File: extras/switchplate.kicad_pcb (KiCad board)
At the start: 2 copper layers, 344.4 x 121.3 mm, 2 parts

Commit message: update gerbers to latest kicad version defaults
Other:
- rule pad_to_mask_clearance: 0.05 -> 0

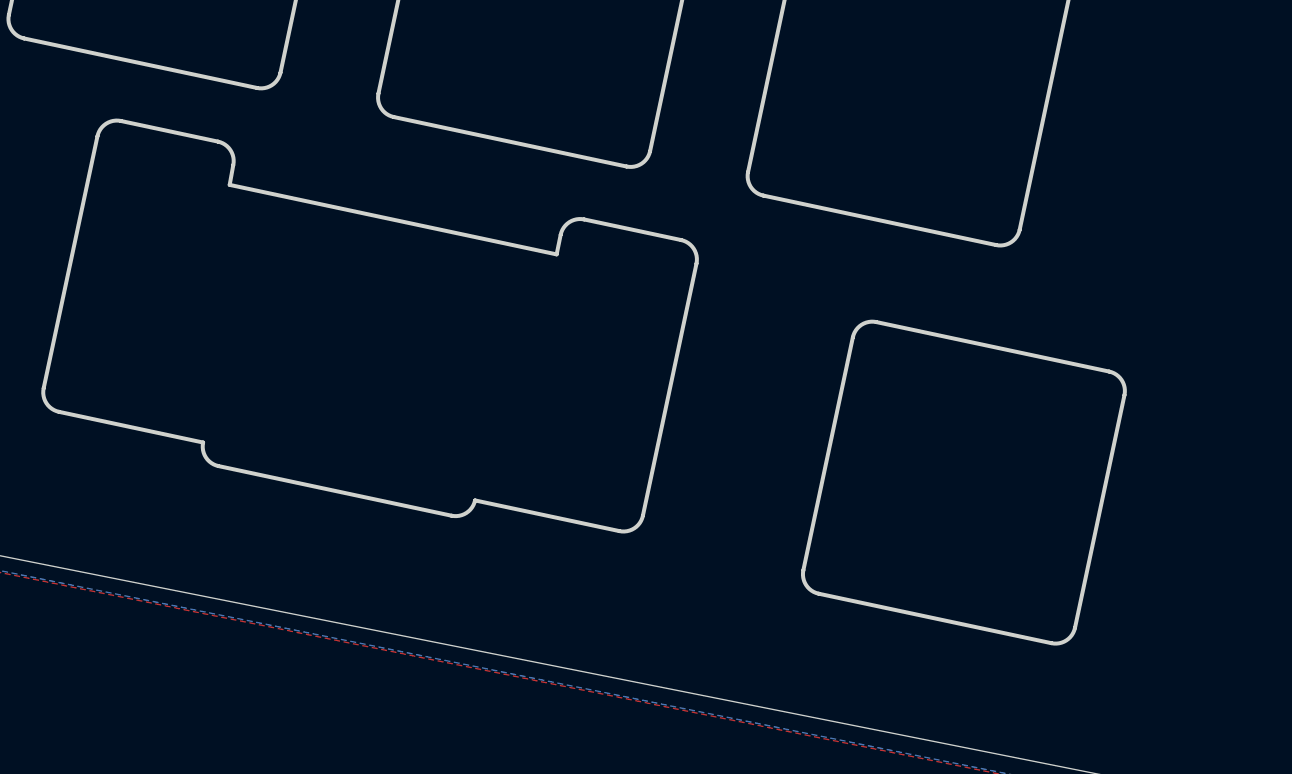
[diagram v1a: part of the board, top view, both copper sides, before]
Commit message: add 2.25u left space support and update caps to use cftkb footprints
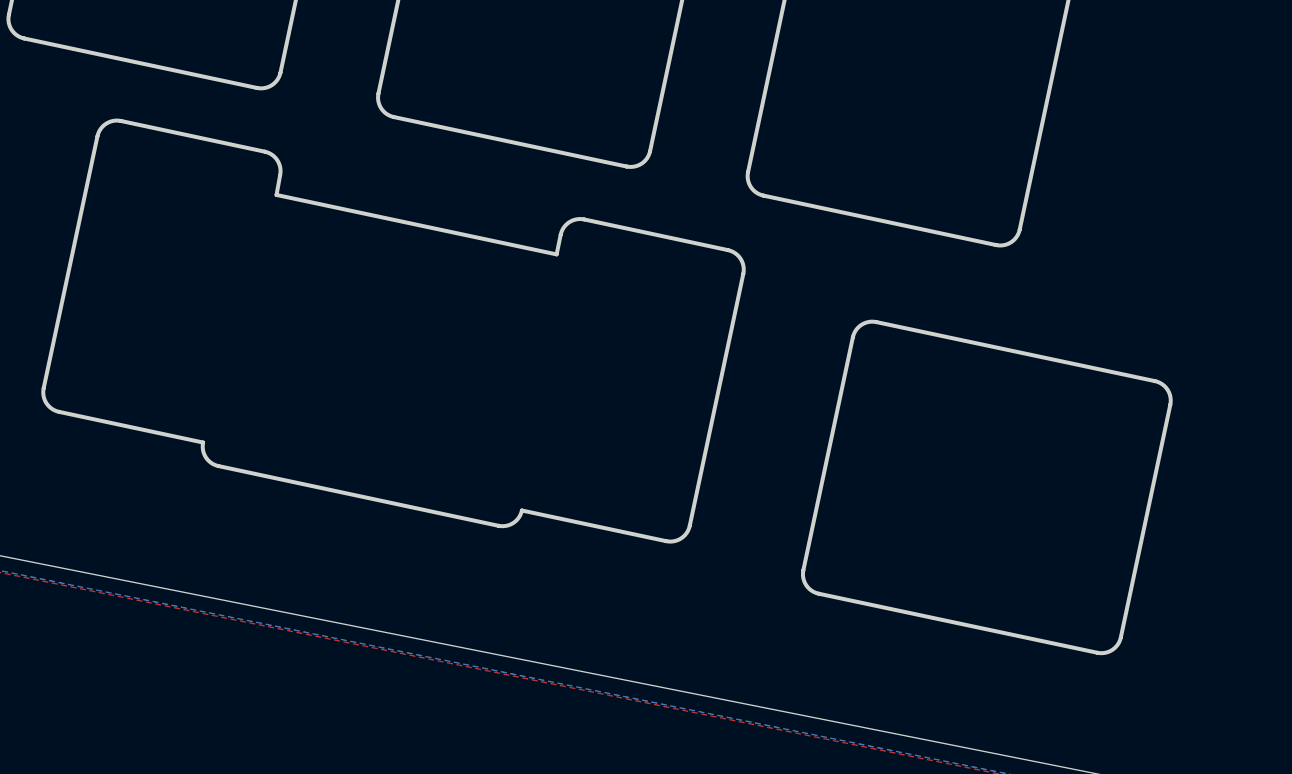
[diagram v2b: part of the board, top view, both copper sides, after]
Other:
- outline, holes or cut-outs redrawn
